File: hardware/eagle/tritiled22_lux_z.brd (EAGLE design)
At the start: 27.9 x 27.9 mm, 15 parts, among them Q1 ZXMN3B01FTA, Q2 DMG2305UX, SW1 SMD_SWITCH, U1 PIC12LF1571

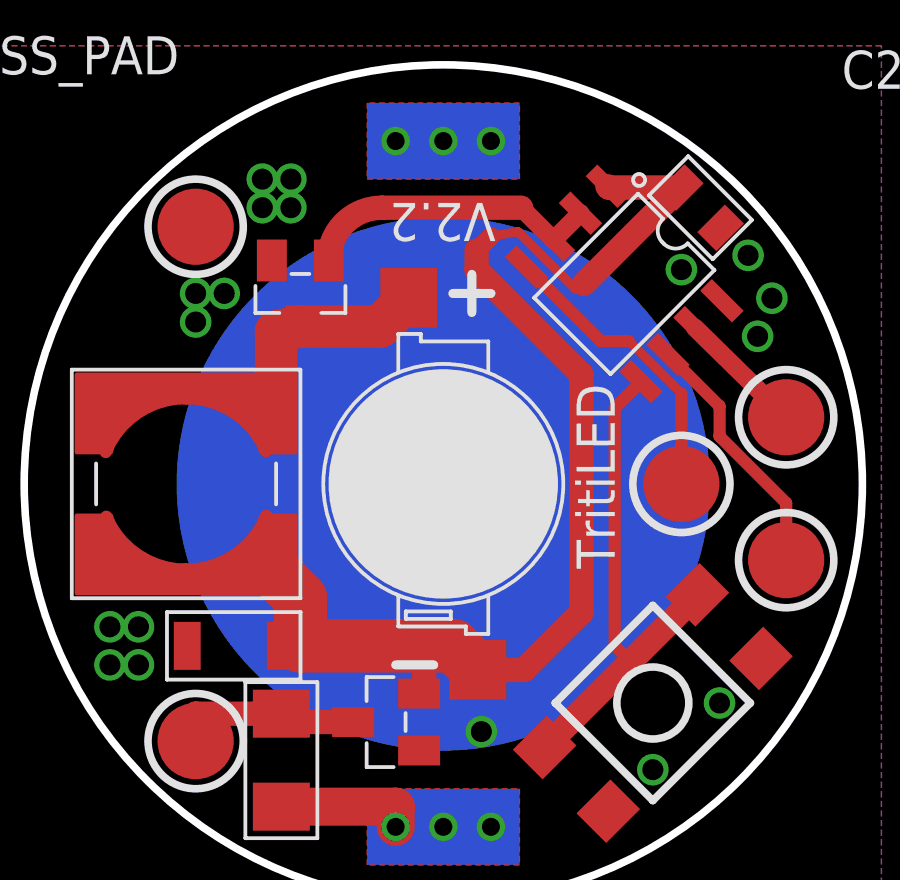
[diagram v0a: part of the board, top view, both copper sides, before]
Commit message: Added new LED eiditons: 5630, Luxeon C, Luxeon Z fixed inconsistent C2 value: now should be 100n everywhere
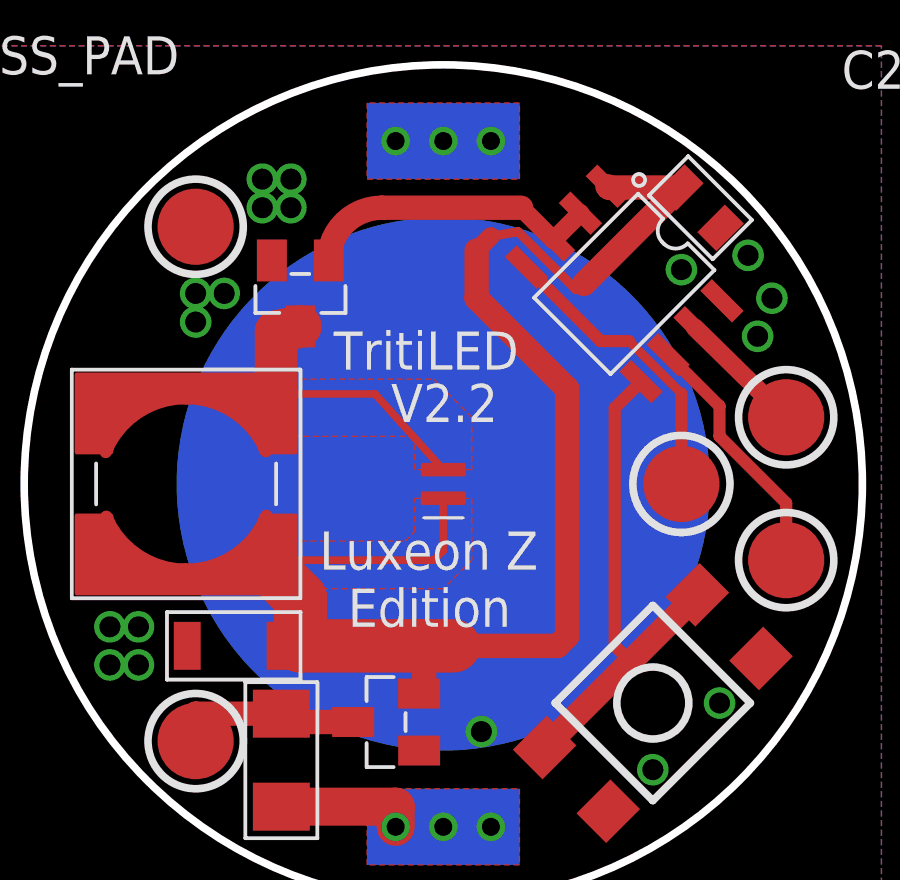
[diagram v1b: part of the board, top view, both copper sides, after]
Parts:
- D1: value Chanzon 3W -> Luxeon Z; device tritiled:LED_3W -> tritiled:LUXEON_Z
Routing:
- net +3.3V: track 41.2 -> 47.7 mm
- net N$5: track 6.91 -> 9.60 mm
- added copper zone on layer 1, net +3.3V
- added copper zone on layer 1, net N$5
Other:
- board text added: "Edition"
- board text added: "Luxeon Z"
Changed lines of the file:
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@@
 <setting verticaltext="up"/>
 </settings>
-<grid distance="0.0125" unitdist="inch" unit="inch" style="lines" multiple="1" display="no" altdistance="0.025" altunitdist="inch" altunit="inch"/>
+<grid distance="0.006125" unitdist="inch" unit="inch" style="lines" multiple="1" display="no" altdistance="0.025" altunitdist="inch" altunit="inch"/>
 <layers>
 <layer number="1" name="Top" color="4" fill="1" visible="yes" active="yes"/>
@@
 <plain>
 <circle x="15.24" y="14.605" radius="13.97" width="0.254" layer="20"/>
-<circle x="15.24" y="14.605" radius="3.82320625" width="0" layer="21"/>
 <circle x="6.985" y="6.0325" radius="1.5875" width="0.254" layer="21"/>
 <circle x="6.985" y="23.1775" radius="1.5875" width="0.254" layer="21"/>
@@
 <circle x="26.67" y="16.8275" radius="1.5875" width="0.254" layer="21"/>
 <circle x="23.1775" y="14.605" radius="1.6189375" width="0.254" layer="21"/>
-<text x="19.685" y="17.93875" size="1.27" layer="21" font="vector" ratio="13" rot="R270">TritiLED</text>
-<text x="16.98625" y="23.97125" size="1.27" layer="21" font="vector" ratio="13" rot="SR180">V2.2</text>
+<text x="11.58875" y="18.415" size="1.27" layer="21" font="vector" ratio="13">TritiLED</text>
+<text x="13.49375" y="16.66875" size="1.27" layer="21" font="vector" ratio="13" rot="SR0">V2.2</text>
 <wire x1="11.43" y1="26.035" x2="11.43" y2="3.175" width="3.81" layer="22" curve="143.130102" cap="flat"/>
 <wire x1="19.05" y1="26.035" x2="19.05" y2="3.175" width="3.81" layer="22" curve="-143.130102" cap="flat"/>
@@
 <wire x1="14.9225" y1="1.27" x2="15.5575" y2="1.27" width="0.3048" layer="22"/>
 <wire x1="15.24" y1="1.5875" x2="15.24" y2="0.9525" width="0.3048" layer="22"/>
-<wire x1="13.6525" y1="8.5725" x2="14.9225" y2="8.5725" width="0.3048" layer="21"/>
-<wire x1="15.5575" y1="20.955" x2="16.8275" y2="20.955" width="0.3048" layer="21"/>
-<wire x1="16.1925" y1="21.59" x2="16.1925" y2="20.32" width="0.3048" layer="21"/>
 <dimension x1="9.8425" y1="5.3975" x2="-0.3175" y2="-0.9525" x3="-0.9525" y3="-1.27" textsize="1.778" layer="48" dtype="leader"/>
 <dimension x1="8.255" y1="9.2075" x2="-4.445" y2="8.5725" x3="-4.445" y3="8.5725" textsize="1.778" layer="48" dtype="leader"/>
@@
 <dimension x1="15.24" y1="14.605" x2="32.385" y2="5.08" x3="32.385" y3="5.08" textsize="1.778" layer="48" dtype="leader"/>
 <dimension x1="6.985" y1="6.0325" x2="-0.9525" y2="3.4925" x3="-0.9525" y3="3.4925" textsize="1.778" layer="48" dtype="leader"/>
+<text x="11.1125" y="11.7475" size="1.27" layer="21" ratio="13">Luxeon Z</text>
+<text x="12.065" y="9.8425" size="1.27" layer="21" ratio="13">Edition</text>
 </plain>
 <attributes>
@@
 <attribute name="VALUE" x="-7.9375" y="14.605" size="1.27" layer="27"/>
 </element>
-<element name="D1" library="tritiled" package="LED_3W" value="Chanzon 3W" x="15.24" y="14.605" smashed="yes" rot="R90">
+<element name="D1" library="tritiled" package="LUXEON_Z" value="Luxeon Z" x="15.24" y="14.605" smashed="yes" rot="R90">
 <attribute name="NAME" x="33.02" y="5.3975" size="1.27" layer="25"/>
 <attribute name="VALUE" x="33.02" y="3.4925" size="1.27" layer="27"/>
@@
 <contactref element="D1" pad="A"/>
 <contactref element="Q1" pad="3"/>
-<wire x1="14.09" y1="20.805" x2="13.14" y2="19.855" width="1.4224" layer="1"/>
-<wire x1="13.14" y1="19.855" x2="10.4775" y2="19.855" width="1.4224" layer="1"/>
 <wire x1="10.4775" y1="19.855" x2="9.6675" y2="19.68" width="1.4224" layer="1"/>
 <wire x1="9.6675" y1="19.68" x2="9.6675" y2="17.605" width="1.4224" layer="1"/>
+<polygon width="0.254" layer="1" thermals="no">
+<vertex x="9.2075" y="18.0975"/>
+<vertex x="14.9225" y="18.0975"/>
+<vertex x="16.1925" y="16.8275"/>
+<vertex x="16.1925" y="15.084425"/>
+<vertex x="14.2875" y="15.084425"/>
+<vertex x="14.2875" y="16.1925"/>
+<vertex x="9.2075" y="16.1925"/>
+</polygon>
+<wire x1="9.6675" y1="17.605" x2="12.965" y2="17.605" width="0.254" layer="1"/>
+<wire x1="12.965" y1="17.605" x2="15.24" y2="15.08" width="0.254" layer="1"/>
 </signal>
 <signal name="+3.3V">
@@
 <contactref element="D1" pad="C"/>
 <wire x1="9.6675" y1="11.605" x2="9.755" y2="11.5175" width="1.778" layer="1"/>
-<wire x1="16.66" y1="8.405" x2="16.39" y2="8.405" width="0.8128" layer="1"/>
-<wire x1="16.35125" y1="21.74875" x2="19.84375" y2="18.25625" width="0.8128" layer="1"/>
-<wire x1="19.84375" y1="18.25625" x2="19.84375" y2="10.31875" width="0.8128" layer="1"/>
-<wire x1="19.84375" y1="10.31875" x2="17.93" y2="8.405" width="0.8128" layer="1"/>
-<wire x1="17.93" y1="8.405" x2="16.39" y2="8.405" width="0.8128" layer="1"/>
 <contactref element="Q2" pad="2"/>
 <contactref element="C1" pad="P$1"/>
 <contactref element="C2" pad="P$1"/>
-<wire x1="16.39" y1="8.405" x2="15.5875" y2="9.2075" width="1.778" layer="1"/>
 <wire x1="15.5875" y1="9.2075" x2="14.605" y2="9.2075" width="1.778" layer="1"/>
 <wire x1="14.605" y1="9.2075" x2="10.4775" y2="9.2075" width="1.778" layer="1"/>
@@
 <wire x1="17.73555" y1="23.0124" x2="16.8275" y2="22.86" width="0.3048" layer="1"/>
 <wire x1="16.8275" y1="22.86" x2="16.35125" y2="22.38375" width="0.6096" layer="1"/>
-<wire x1="16.35125" y1="22.38375" x2="16.35125" y2="21.74875" width="0.8128" layer="1"/>
 <wire x1="14.435" y1="7.6175" x2="14.605" y2="7.6175" width="0.8128" layer="1"/>
 <wire x1="14.605" y1="7.6175" x2="14.605" y2="9.2075" width="0.8128" layer="1"/>
 <wire x1="9.805" y1="9.2075" x2="10.4775" y2="9.2075" width="0.6096" layer="1"/>
+<wire x1="16.35125" y1="20.79625" x2="19.3675" y2="17.78" width="0.8128" layer="1"/>
+<wire x1="19.3675" y1="17.78" x2="19.3675" y2="9.525" width="0.8128" layer="1"/>
+<wire x1="19.3675" y1="9.525" x2="19.05" y2="9.2075" width="0.8128" layer="1"/>
+<wire x1="19.05" y1="9.2075" x2="15.5875" y2="9.2075" width="0.8128" layer="1"/>
+<wire x1="16.35125" y1="22.38375" x2="16.35125" y2="20.79625" width="0.8128" layer="1"/>
+<polygon width="0.254" layer="1" thermals="no">
+<vertex x="14.2875" y="14.125575"/>
+<vertex x="16.1925" y="14.125575"/>
+<vertex x="16.1925" y="12.065"/>
+<vertex x="15.24" y="11.1125"/>
+<vertex x="9.2075" y="11.1125"/>
+<vertex x="9.2075" y="12.7"/>
+<vertex x="13.97" y="12.7"/>
+<vertex x="14.2875" y="13.0175"/>
+</polygon>
+<wire x1="15.24" y1="14.13" x2="15.24" y2="12.3825" width="0.254" layer="1"/>
+<wire x1="15.24" y1="12.3825" x2="14.9225" y2="12.065" width="0.254" layer="1"/>
+<wire x1="14.9225" y1="12.065" x2="10.1275" y2="12.065" width="0.254" layer="1"/>
+<wire x1="10.1275" y1="12.065" x2="9.6675" y2="11.605" width="0.254" layer="1"/>
 </signal>
 <signal name="N$7">
